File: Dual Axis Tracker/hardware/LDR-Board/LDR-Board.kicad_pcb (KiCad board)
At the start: 2 copper layers, 29.2 x 40.6 mm, 7 parts, among them J1 TO SOLAR SHIELD

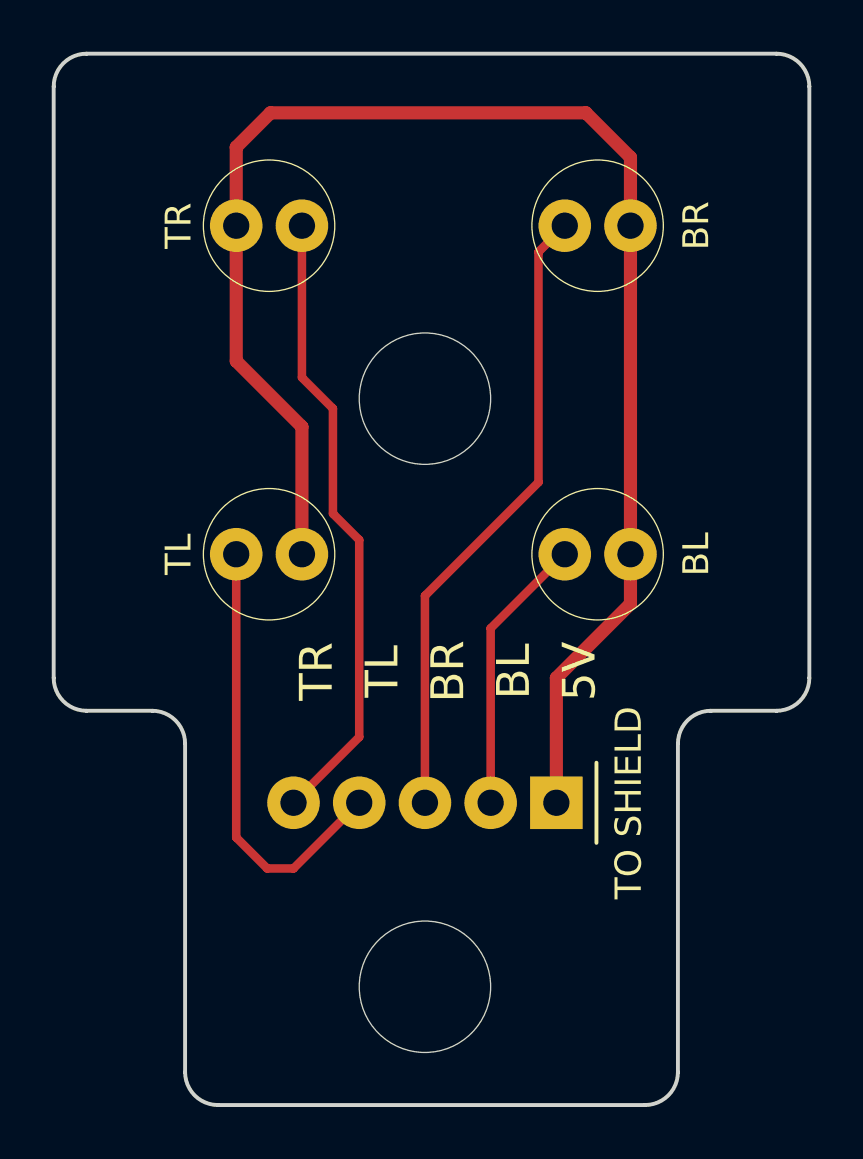
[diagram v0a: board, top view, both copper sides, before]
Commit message: Release v1.3 LDR Board, wider photocell pins
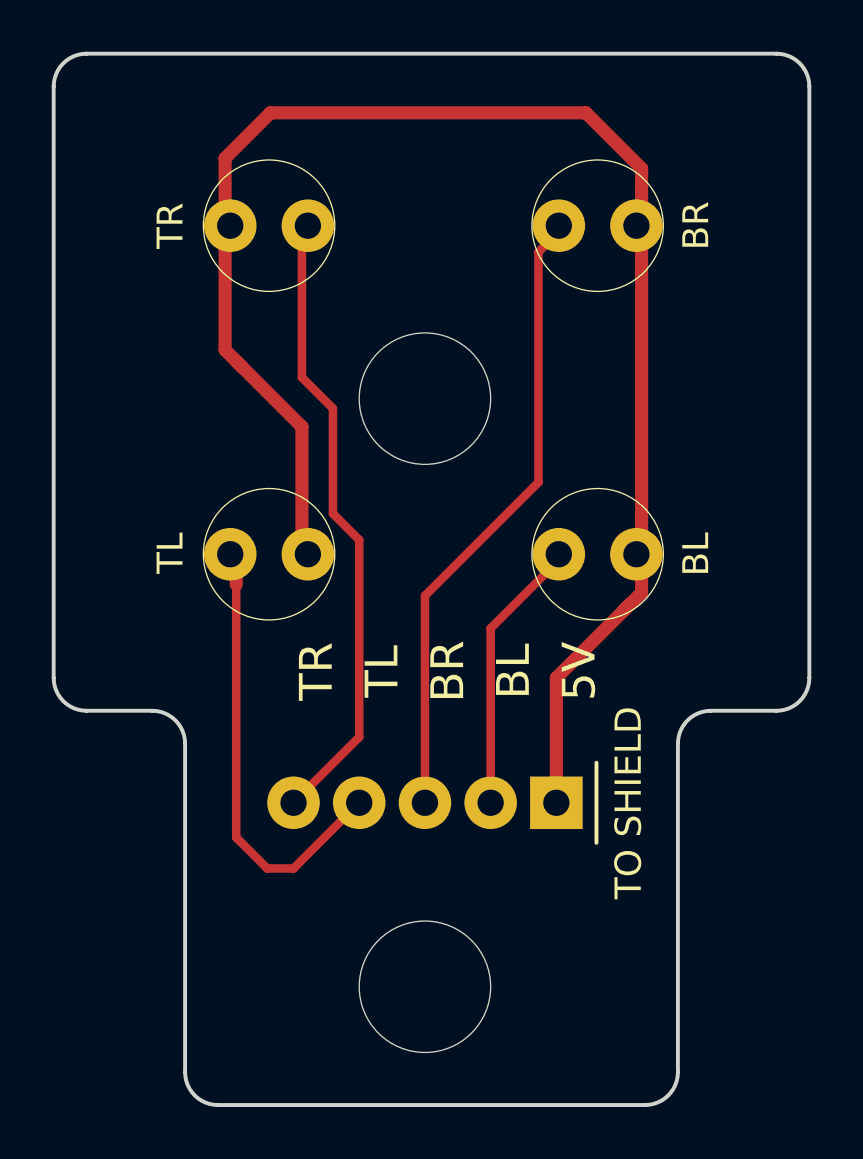
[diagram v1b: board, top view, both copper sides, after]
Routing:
- net +5V: track 59.4 -> 60.8 mm
- net /TOPLEFT: track 17.3 -> 18.6 mm
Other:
- board text added: "LDR Board v1.3"
- board text removed: "LDR Board v1.2"

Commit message: Generate gerbers for v 1.3.1
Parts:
- J1: footprint Wickerlib:CONN-ONSHORE-SCREW-GREEN-5PIN-TH -> LDR-Board:CONN-ONSHORE-SCREW-GREEN-5PIN-TH
- R1, R2, R3, R4: footprint Wickerlib:PHOTOCELL-5.1MM -> LDR-Board:PHOTOCELL-5.1MM
